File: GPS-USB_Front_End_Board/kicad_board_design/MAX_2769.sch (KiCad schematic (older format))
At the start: 47 parts, among them J3 Edge Launch SMA, U4 MAX8510, U5 MAX8510, U6 MAX2769CETI+, U7 SAWTEK-855969, U8 LT1719S6 -- Not Populated, X1 13.368MHz TCXO

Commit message: Fix footprint for MAX 8510 (two places).
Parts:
- U4, U5: footprint rf:21-0076E -> rf:21-0076E_FLIP
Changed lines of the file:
@@
 F 0 "U4" H 8392 5110 50  0000 L BNN
 F 1 "MAX8510" H 8365 5009 50  0000 L BNN
-F 2 "rf:21-0076E" H 7375 4750 50  0001 L BNN
+F 2 "rf:21-0076E_FLIP" H 7375 4750 50  0001 L BNN
 F 3 "None" H 7375 4750 50  0001 L BNN
 F 4 "Unavailable" H 7375 4750 50  0001 L BNN "Field4"
@@
 F 0 "U5" H 8392 6160 50  0000 L BNN
 F 1 "MAX8510" H 8365 6059 50  0000 L BNN
-F 2 "rf:21-0076E" H 7375 5800 50  0001 L BNN
+F 2 "rf:21-0076E_FLIP" H 7375 5800 50  0001 L BNN
 F 3 "None" H 7375 5800 50  0001 L BNN
 F 4 "Unavailable" H 7375 5800 50  0001 L BNN "Field4"

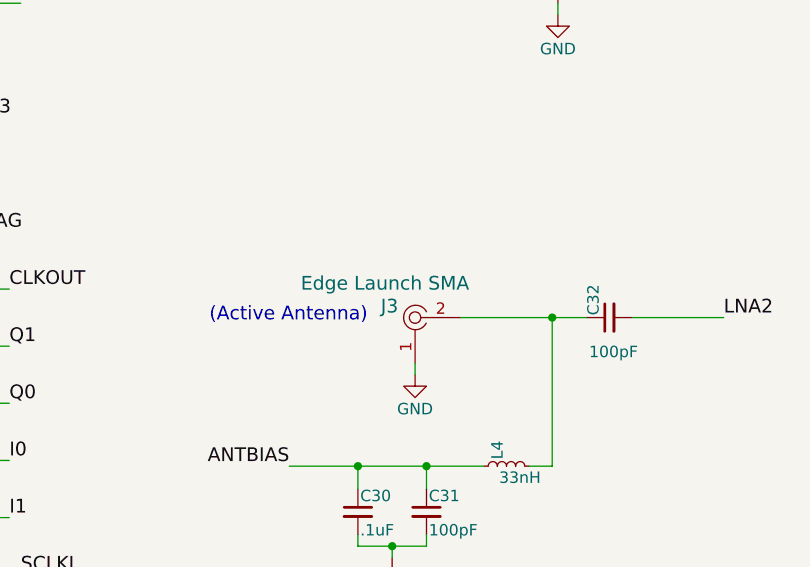
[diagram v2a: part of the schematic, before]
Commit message: Change out SMA connector for thru-hole version.
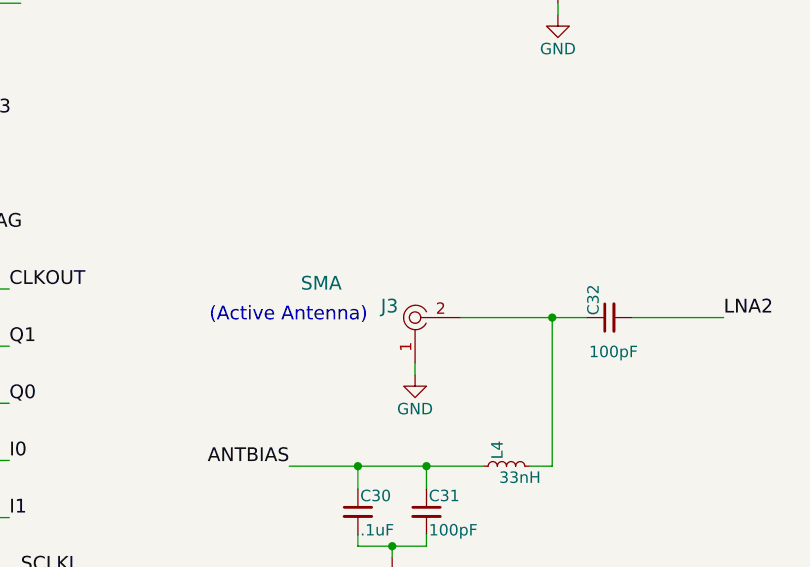
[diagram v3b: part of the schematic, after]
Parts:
- J3: value Edge Launch SMA -> SMA; footprint digikey-footprints:RF_SMA_Receptical_Vertical_CONSMA001-SMD-G -> digikey-footprints:RF_SMA_Vertical_5-1814832-1; Digi-Key_PN CONSMA001-SMD-G-ND -> A97594-ND; MPN CONSMA001-SMD-G -> 5-1814832-1; Manufacturer Linx Technologies Inc. -> TE Connectivity AMP Connectors
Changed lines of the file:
@@
 P 4100 5375
 F 0 "J3" H 3950 5425 60  0000 L CNN
-F 1 "Edge Launch SMA" H 3600 5525 60  0000 L CNN
-F 2 "digikey-footprints:RF_SMA_Receptical_Vertical_CONSMA001-SMD-G" H 4300 5575 60  0001 L CNN
-F 3 "https://linxtechnologies.com/wp/wp-content/uploads/consma001-smd-g.pdf" H 4300 5675 60  0001 L CNN
-F 4 "CONSMA001-SMD-G-ND" H 4300 5775 60  0001 L CNN "Digi-Key_PN"
-F 5 "CONSMA001-SMD-G" H 4300 5875 60  0001 L CNN "MPN"
+F 1 "SMA" H 3600 5525 60  0000 L CNN
+F 2 "digikey-footprints:RF_SMA_Vertical_5-1814832-1" H 4300 5575 60  0001 L CNN
+F 3 "https://www.te.com/commerce/DocumentDelivery/DDEController?Action=srchrtrv&DocNm=1814832&DocType=Customer+Drawing&DocLang=English" H 4300 5675 60  0001 L CNN
+F 4 "A97594-ND" H 4300 5775 60  0001 L CNN "Digi-Key_PN"
+F 5 "5-1814832-1" H 4300 5875 60  0001 L CNN "MPN"
 F 6 "Connectors, Interconnects" H 4300 5975 60  0001 L CNN "Category"
 F 7 "Coaxial Connectors (RF)" H 4300 6075 60  0001 L CNN "Family"
@@
 F 9 "/product-detail/en/linx-technologies-inc/CONSMA001-SMD-G/CONSMA001-SMD-G-ND/4496569" H 4300 6275 60  0001 L CNN "DK_Detail_Page"
 F 10 "CONN SMA RCPT STR 50 OHM SMD" H 4300 6375 60  0001 L CNN "Description"
-F 11 "Linx Technologies Inc." H 4300 6475 60  0001 L CNN "Manufacturer"
+F 11 "TE Connectivity AMP Connectors" H 4300 6475 60  0001 L CNN "Manufacturer"
 F 12 "Active" H 4300 6575 60  0001 L CNN "Status"
 F 13 "Linx Technologies" H 0   0   50  0001 C CNN "MFR"

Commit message: Update to MAX2771.  Changes to decoupling caps, Remove ANTFLAG, IDLE signals.  Add explicit antenna bias.  New matching network for LNA input.  Remove bypass for SAW filter.
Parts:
- removed C29: NC, Capacitors_SMD:C_0805_HandSoldering, symbol C_Small
- removed R11: NC, Resistors_SMD:R_0805_HandSoldering, symbol R
- removed R12: 0, Resistors_SMD:R_0805_HandSoldering, symbol R
- removed U6: MAX2769CETI+, rf:TQFP_29_EP_MAX2769, symbol MAX2769CETI+
- added C?: .47nF, Capacitors_SMD:C_0603_HandSoldering, symbol C_Small
- added C?: 1.7pF, Capacitors_SMD:C_0805_HandSoldering, symbol C_Small
- added L?: 5.6nH, Capacitors_SMD:C_0402, symbol L_Small
- added P?: CONN_01X03, symbol CONN_01X03
- added U?: MAX2771, QFN50P500X500X80-29N, symbol MAX2771
- added W?: -BB, Measurement_Points:Measurement_Point_Round-TH_Small, symbol TEST_1P
- added W?: +BB, Measurement_Points:Measurement_Point_Round-TH_Small, symbol TEST_1P
- C19: footprint Capacitors_SMD:C_0805_HandSoldering -> Capacitors_SMD:C_0402
- C23, C36: value .1uF -> 2.2uF; footprint Capacitors_SMD:C_0402 -> Capacitors_SMD:C_0603
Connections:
- net labels removed: ANTBIAS, ANTFLAG, IDLE#, LNA2
- wire segments 151 -> 185
- no-connect marks 4 -> 7
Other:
- moved on the sheet: C11, C20, C30, C31, C32, J3, L4, R10, R14, R15, R16, R17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

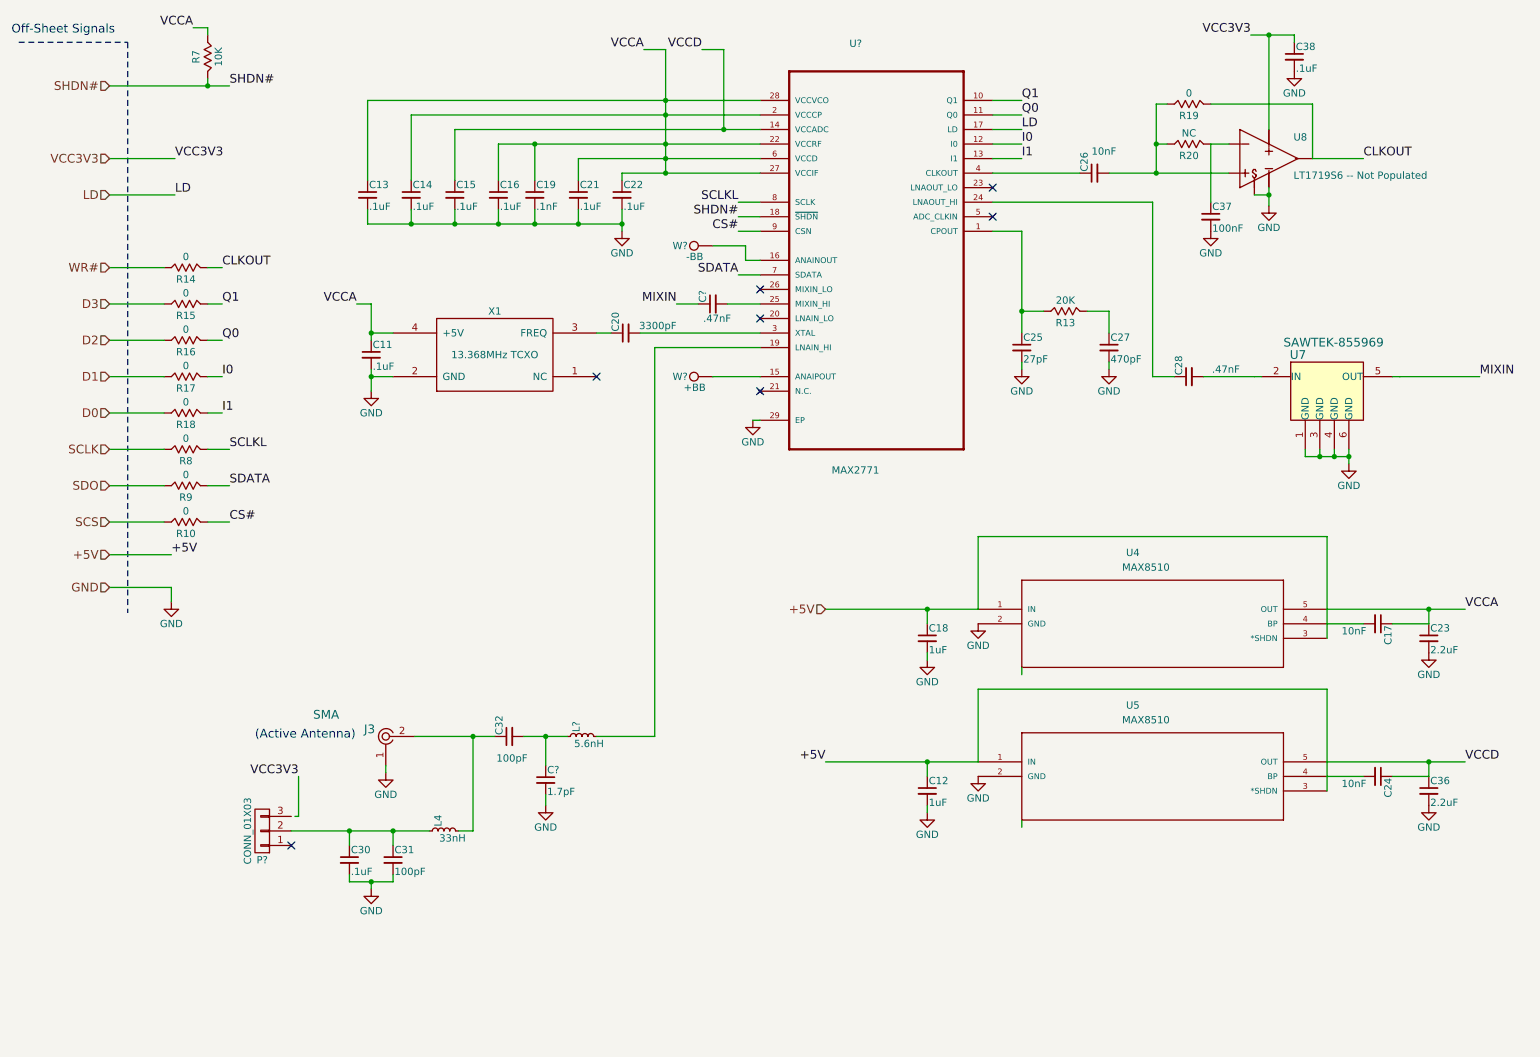
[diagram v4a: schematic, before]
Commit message: Add some footprints, annotate new parts, generate netlist, EDR check.
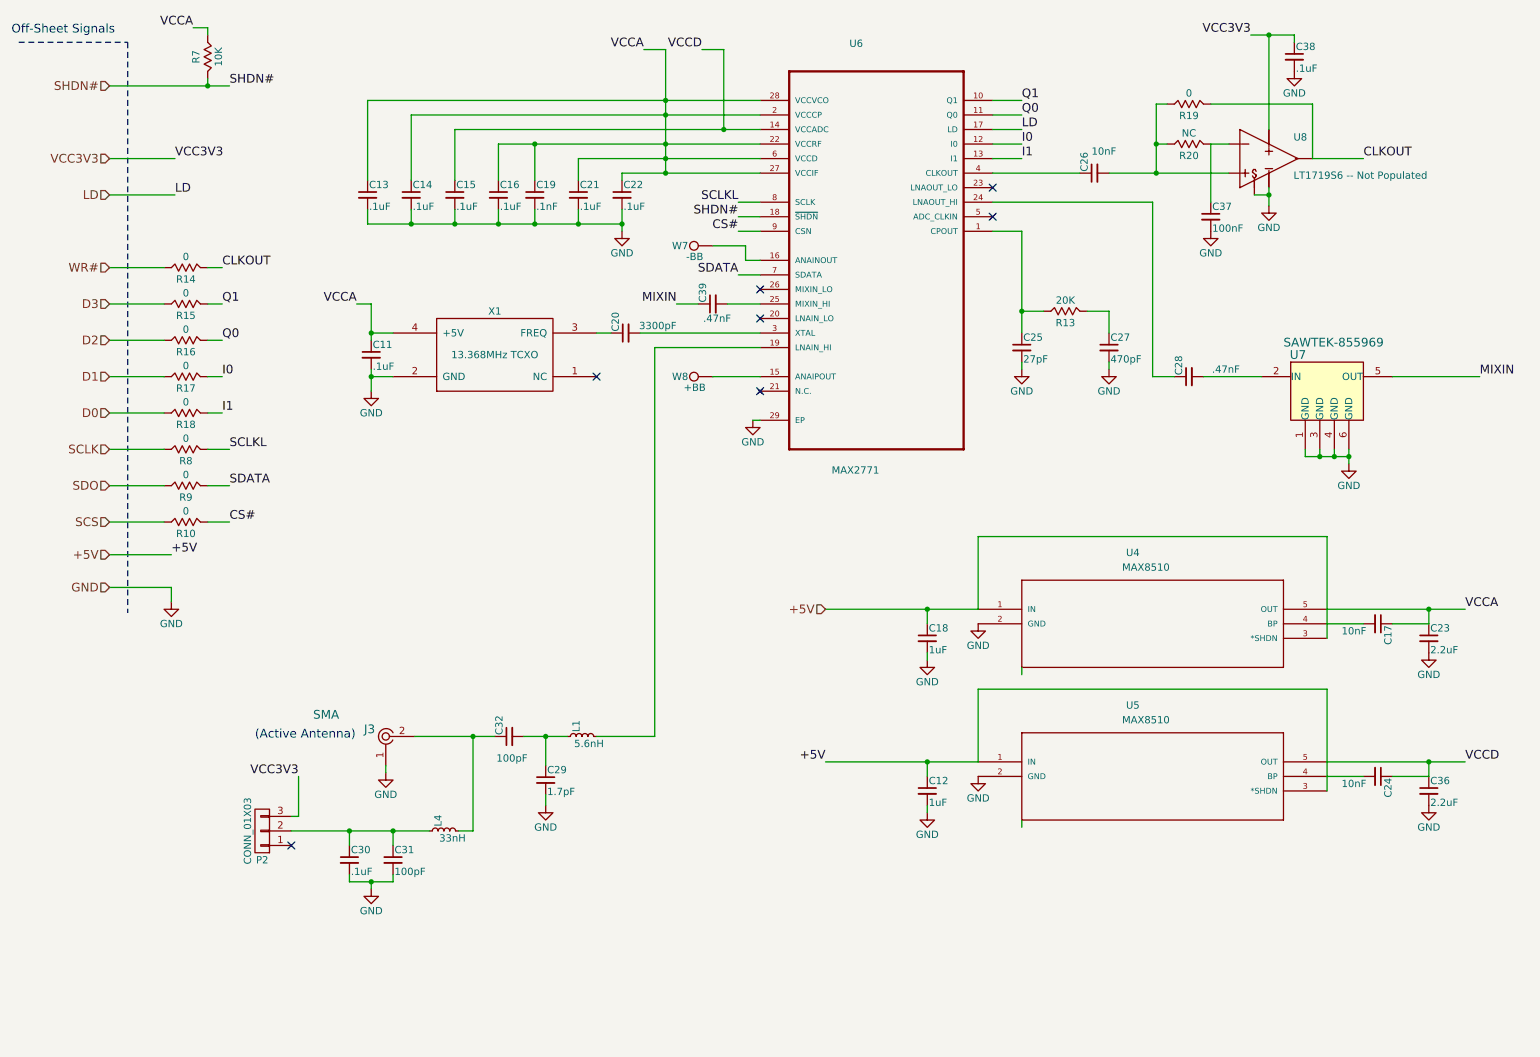
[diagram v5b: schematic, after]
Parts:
- C23, C36: footprint Capacitors_SMD:C_0603 -> Capacitors_SMD:C_0805; MFR TDK -> Samsung; MPN CGA2B1X7R1C104K050BC -> CL21B225KPFNNNE; SPN 445-5613-1-ND -> 1276-1188-1-ND
- C29: renamed from C?; footprint Capacitors_SMD:C_0805_HandSoldering -> Capacitors_SMD:C_0402; MFR Kemet -> Murata; MPN C0805C101K4RAC7800 -> GJM1555C1H1R7WB01D; SPN 399-15003-1-ND -> 490-11201-1-ND
- C39: renamed from C?; MFR AVX -> Kemet; MPN 06035C332KAT4A -> C0603C471K5RACTU; SPN 478-10681-1-ND -> 399-1075-1-ND
- L1: renamed from L?; MFR Bourns -> Johansen Technology; MPN CI100505-33NJ -> L-07C5N6SV6T; SPN CI100505-33NJCT-ND -> 712-1462-1-ND
- P2: renamed from P?; footprint (none) -> Connectors_Molex:Molex_KK-6410-03_03x2.54mm_Straight
- U6: renamed from U?; footprint QFN50P500X500X80-29N -> rf:TQFP_29_EP_MAX2769
- gave numbers to parts that had none: 2
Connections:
- net VCC3V3: now also P2.3 (P3)

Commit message: Intermediate routing.
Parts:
- C31, C32: footprint Capacitors_SMD:C_0805_HandSoldering -> Capacitors_SMD:C_0402; MFR Kemet -> Yageo; MPN C0805C101K4RAC7800 -> CC0402JRNPO9BN101; SPN 399-15003-1-ND -> 311-1024-1-ND
- C39: footprint Capacitors_SMD:C_0603_HandSoldering -> Capacitors_SMD:C_0402; MFR Kemet -> AVX; MPN C0603C471K5RACTU -> 04025C471KAT2A; SPN 399-1075-1-ND -> 478-1097-1-ND
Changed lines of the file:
@@
 F 0 "C32" H 4160 5695 50  0000 L CNN
 F 1 "100pF" V 4000 5500 50  0000 L CNN
-F 2 "Capacitors_SMD:C_0805_HandSoldering" H 4150 5625 50  0001 C CNN
+F 2 "Capacitors_SMD:C_0402" H 4150 5625 50  0001 C CNN
 F 3 "" H 4150 5625 50  0001 C CNN
-F 4 "Kemet" H -800 250 50  0001 C CNN "MFR"
-F 5 "C0805C101K4RAC7800" H -800 250 50  0001 C CNN "MPN"
+F 4 "Yageo" H -800 250 50  0001 C CNN "MFR"
+F 5 "CC0402JRNPO9BN101" H -800 250 50  0001 C CNN "MPN"
 F 6 "Digikey" H -800 250 50  0001 C CNN "SPR"
-F 7 "399-15003-1-ND" H -800 250 50  0001 C CNN "SPN"
+F 7 "311-1024-1-ND" H -800 250 50  0001 C CNN "SPN"
 F 8 "-" H -800 250 50  0001 C CNN "SPURL"
 	1    4150 5625
 	0    -1   -1   0
-$EndComp
-$Comp
-L C_Small C31
-U 1 1 5B23B2CD
-P 3350 6475
-F 0 "C31" H 3360 6545 50  0000 L CNN
-F 1 "100pF" H 3360 6395 50  0000 L CNN
-F 2 "Capacitors_SMD:C_0805_HandSoldering" H 3350 6475 50  0001 C CNN
-F 3 "" H 3350 6475 50  0001 C CNN
-F 4 "Kemet" H -800 250 50  0001 C CNN "MFR"
-F 5 "C0805C101K4RAC7800" H -800 250 50  0001 C CNN "MPN"
-F 6 "Digikey" H -800 250 50  0001 C CNN "SPR"
-F 7 "399-15003-1-ND" H -800 250 50  0001 C CNN "SPN"
-F 8 "-" H -800 250 50  0001 C CNN "SPURL"
-	1    3350 6475
-	1    0    0    -1
 $EndComp
 $Comp
@@
 Text Label 1850 1900 0    60   ~ 0
 LD
-$Comp
-L C_Small C39
-U 1 1 5D3BF52B
-P 5550 2650
-F 0 "C39" H 5560 2720 50  0000 L CNN
-F 1 ".47nF" V 5450 2525 50  0000 L CNN
-F 2 "Capacitors_SMD:C_0603_HandSoldering" H 5550 2650 50  0001 C CNN
-F 3 "" H 5550 2650 50  0001 C CNN
-F 4 "Kemet" H 1075 -200 50  0001 C CNN "MFR"
-F 5 "C0603C471K5RACTU" H 1075 -200 50  0001 C CNN "MPN"
-F 6 "Digikey" H 1075 -200 50  0001 C CNN "SPR"
-F 7 "399-1075-1-ND" H 1075 -200 50  0001 C CNN "SPN"
-F 8 "-" H 1075 -200 50  0001 C CNN "SPURL"
-	1    5550 2650
-	0    -1   -1   0
-$EndComp
 Wire Wire Line
 	5450 2650 5300 2650
@@
 Wire Wire Line
 	2700 6175 2700 5900
+$Comp
+L C_Small C39
+U 1 1 5D3D9921
+P 5550 2650
+F 0 "C39" H 5560 2720 50  0000 L CNN
+F 1 ".47nF" V 5600 2300 50  0000 L CNN
+F 2 "Capacitors_SMD:C_0402" H 5550 2650 50  0001 C CNN
+F 3 "" H 5550 2650 50  0001 C CNN
+F 4 "AVX" H -3275 -500 50  0001 C CNN "MFR"
+F 5 "04025C471KAT2A" H -3275 -500 50  0001 C CNN "MPN"
+F 6 "Digikey" H -3275 -500 50  0001 C CNN "SPR"
+F 7 "478-1097-1-ND" H -3275 -500 50  0001 C CNN "SPN"
+F 8 "-" H -3275 -500 50  0001 C CNN "SPURL"
+	1    5550 2650
+	0    -1   -1   0
+$EndComp
+$Comp
+L C_Small C31
+U 1 1 5D3DDB42
+P 3350 6475
+F 0 "C31" H 3360 6545 50  0000 L CNN
+F 1 "100pF" H 3375 6400 50  0000 L CNN
+F 2 "Capacitors_SMD:C_0402" H 3350 6475 50  0001 C CNN
+F 3 "" H 3350 6475 50  0001 C CNN
+F 4 "Yageo" H -1600 1100 50  0001 C CNN "MFR"
+F 5 "CC0402JRNPO9BN101" H -1600 1100 50  0001 C CNN "MPN"
+F 6 "Digikey" H -1600 1100 50  0001 C CNN "SPR"
+F 7 "311-1024-1-ND" H -1600 1100 50  0001 C CNN "SPN"
+F 8 "-" H -1600 1100 50  0001 C CNN "SPURL"
+	1    3350 6475
+	1    0    0    -1
+$EndComp
 $EndSCHEMATC

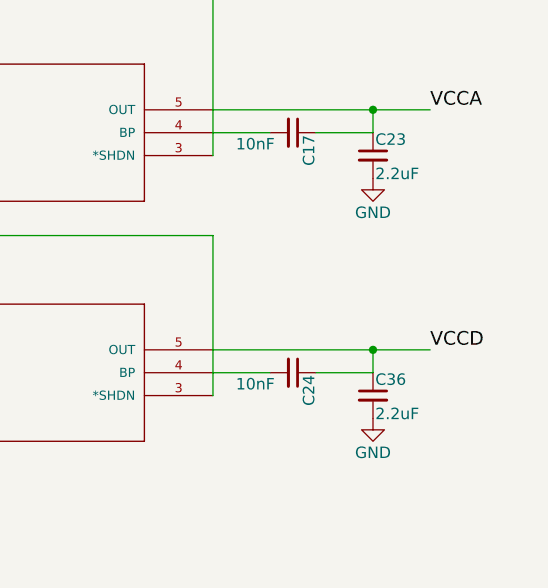
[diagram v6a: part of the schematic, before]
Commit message: Changed 2.2uF to 10uF. Completed routing. Added via fencing and footprint vias.
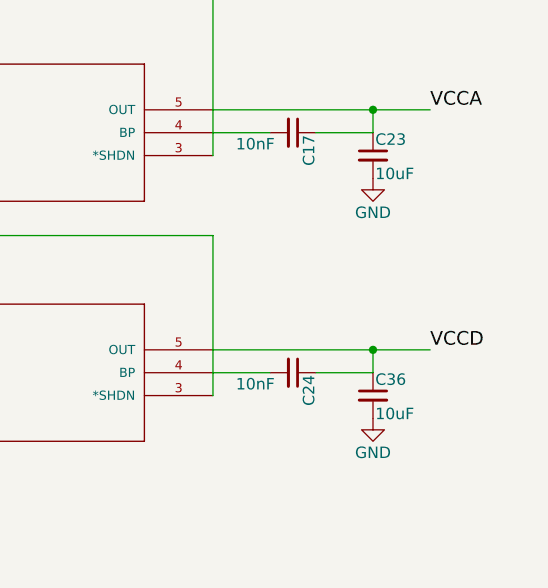
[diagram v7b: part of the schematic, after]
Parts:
- C23, C36: value 2.2uF -> 10uF; MPN CL21B225KPFNNNE -> CL21A106KPFNNNG; SPN 1276-1188-1-ND -> 1276-6456-1-ND
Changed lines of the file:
@@
 P 10475 4950
 F 0 "C23" H 10485 5020 50  0000 L CNN
-F 1 "2.2uF" H 10485 4870 50  0000 L CNN
+F 1 "10uF" H 10485 4870 50  0000 L CNN
 F 2 "Capacitors_SMD:C_0805" H 10475 4950 50  0001 C CNN
 F 3 "" H 10475 4950 50  0001 C CNN
 F 4 "Samsung" H 0   0   50  0001 C CNN "MFR"
-F 5 "CL21B225KPFNNNE" H 0   0   50  0001 C CNN "MPN"
+F 5 "CL21A106KPFNNNG" H 0   0   50  0001 C CNN "MPN"
 F 6 "Digikey" H 0   0   50  0001 C CNN "SPR"
-F 7 "1276-1188-1-ND" H 0   0   50  0001 C CNN "SPN"
+F 7 "1276-6456-1-ND" H 0   0   50  0001 C CNN "SPN"
 F 8 "-" H 0   0   50  0001 C CNN "SPURL"
 	1    10475 4950
@@
 Wire Wire Line
 	10225 3150 10825 3150
-$Comp
-L C_Small C36
-U 1 1 5D3CE3C2
-P 10475 6000
-F 0 "C36" H 10485 6070 50  0000 L CNN
-F 1 "2.2uF" H 10485 5920 50  0000 L CNN
-F 2 "Capacitors_SMD:C_0805" H 10475 6000 50  0001 C CNN
-F 3 "" H 10475 6000 50  0001 C CNN
-F 4 "Samsung" H 0   1050 50  0001 C CNN "MFR"
-F 5 "CL21B225KPFNNNE" H 0   1050 50  0001 C CNN "MPN"
-F 6 "Digikey" H 0   1050 50  0001 C CNN "SPR"
-F 7 "1276-1188-1-ND" H 0   1050 50  0001 C CNN "SPN"
-F 8 "-" H 0   1050 50  0001 C CNN "SPURL"
-	1    10475 6000
-	1    0    0    -1
-$EndComp
 Wire Wire Line
 	2650 6175 2700 6175
@@
 	1    0    0    -1
 $EndComp
+$Comp
+L C_Small C36
+U 1 1 5D3FA7A9
+P 10475 6000
+F 0 "C36" H 10485 6070 50  0000 L CNN
+F 1 "10uF" H 10485 5920 50  0000 L CNN
+F 2 "Capacitors_SMD:C_0805" H 10475 6000 50  0001 C CNN
+F 3 "" H 10475 6000 50  0001 C CNN
+F 4 "Samsung" H 0   1050 50  0001 C CNN "MFR"
+F 5 "CL21A106KPFNNNG" H 0   1050 50  0001 C CNN "MPN"
+F 6 "Digikey" H 0   1050 50  0001 C CNN "SPR"
+F 7 "1276-6456-1-ND" H 0   1050 50  0001 C CNN "SPN"
+F 8 "-" H 0   1050 50  0001 C CNN "SPURL"
+	1    10475 6000
+	1    0    0    -1
+$EndComp

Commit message: Final cleanup before submit to OSHPARK.
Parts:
- renumbered C18 to C12, C24 to C17, C12 to C18, C17 to C24
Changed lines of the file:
@@
 $EndComp
 $Comp
-L C_Small C18
+L C_Small C12
 U 1 1 5B2B7313
 P 7025 4950
-F 0 "C18" H 7035 5020 50  0000 L CNN
+F 0 "C12" H 7035 5020 50  0000 L CNN
 F 1 "1uF" H 7035 4870 50  0000 L CNN
 F 2 "Capacitors_SMD:C_0603_HandSoldering" H 7025 4950 50  0001 C CNN
@@
 $EndComp
 $Comp
-L C_Small C17
+L C_Small C24
 U 1 1 5B5DF4D0
 P 10125 4850
-F 0 "C17" H 10135 4920 50  0000 L CNN
+F 0 "C24" H 10135 4920 50  0000 L CNN
 F 1 "10nF" V 10175 4600 50  0000 L CNN
 F 2 "Capacitors_SMD:C_0402" H 10125 4850 50  0001 C CNN
@@
 $EndComp
 $Comp
-L C_Small C12
+L C_Small C18
 U 1 1 5B5E057D
 P 7025 6000
-F 0 "C12" H 7035 6070 50  0000 L CNN
+F 0 "C18" H 7035 6070 50  0000 L CNN
 F 1 "1uF" H 7035 5920 50  0000 L CNN
 F 2 "Capacitors_SMD:C_0603_HandSoldering" H 7025 6000 50  0001 C CNN
@@
 $EndComp
 $Comp
-L C_Small C24
+L C_Small C17
 U 1 1 5B5E05AD
 P 10125 5900
-F 0 "C24" H 10135 5970 50  0000 L CNN
+F 0 "C17" H 10135 5970 50  0000 L CNN
 F 1 "10nF" V 10175 5650 50  0000 L CNN
 F 2 "Capacitors_SMD:C_0402" H 10125 5900 50  0001 C CNN
